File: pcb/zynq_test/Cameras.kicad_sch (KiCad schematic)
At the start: 0 parts

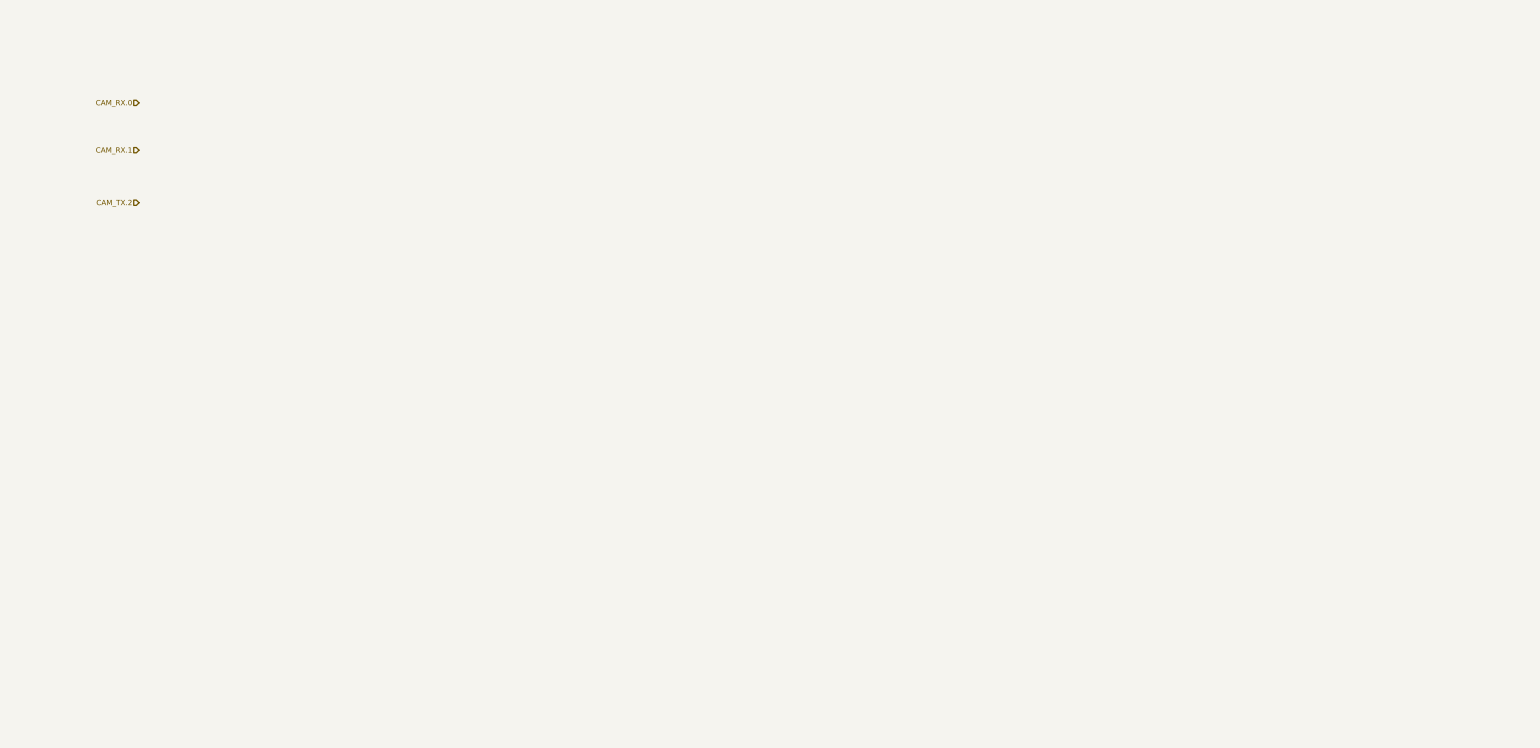
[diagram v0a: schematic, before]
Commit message: Added Cameras, changed SD card IC for skew reasons
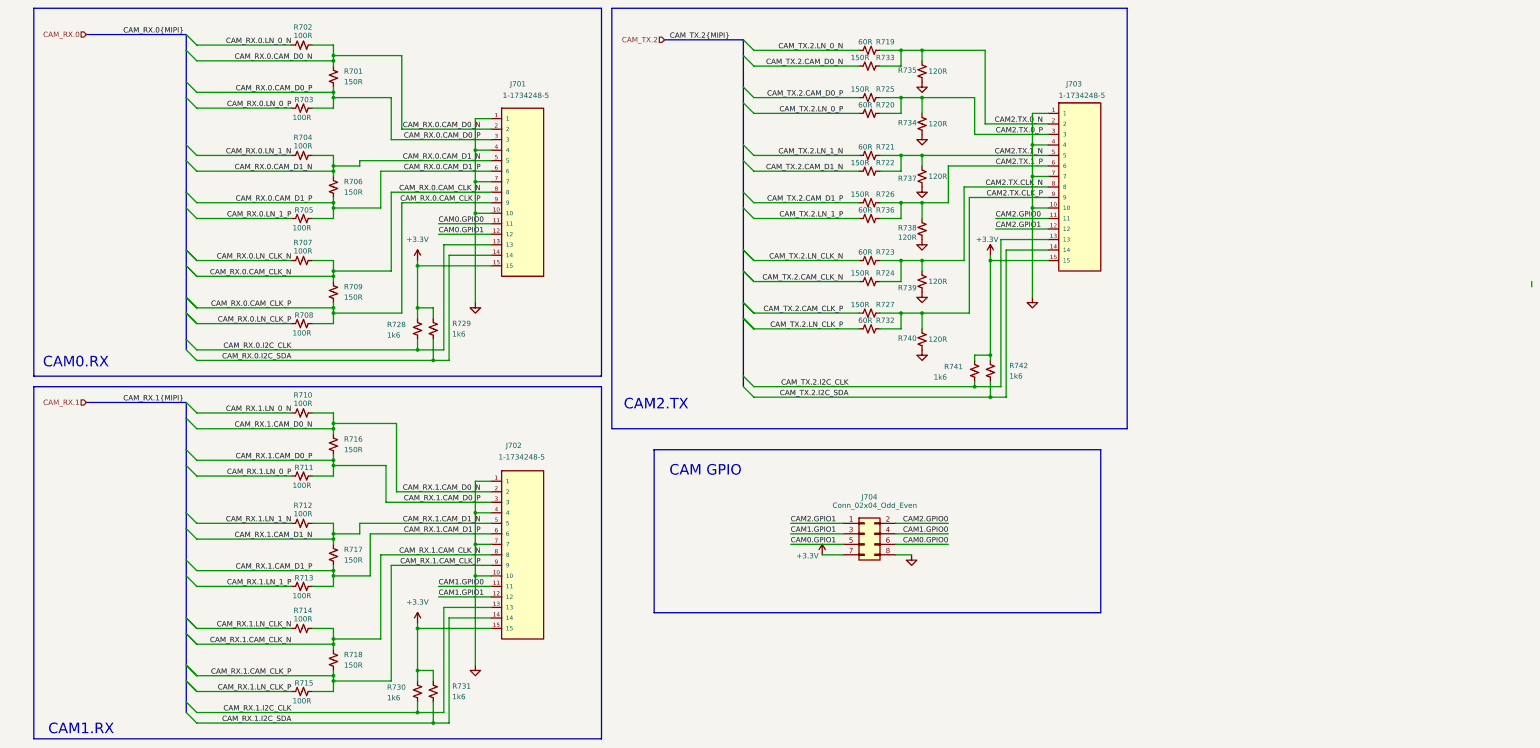
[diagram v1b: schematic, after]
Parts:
- added J701, J702, J703: 1-1734248-5, Camera:TE_1-1734248-5, symbol camera:1-1734248-5
- added J704: Conn_02x04_Odd_Even, symbol Connector_Generic:Conn_02x04_Odd_Even
- added R701, R706, R709, R716, R717, R718, R722, R724, R725, R726, R727, R733: 150R, symbol Device:R_Small_US
- added R702, R703, R704, R705, R707, R708, R710, R711, R712, R713, R714, R715: 100R, symbol Device:R_Small_US
- added R719, R720, R721, R723, R732, R736: 60R, symbol Device:R_Small_US
- added R728, R729, R730, R731, R741, R742: 1k6, symbol Device:R_Small_US
- added R734, R735, R737, R738, R739, R740: 120R, symbol Device:R_Small_US
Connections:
- new net +3.3V: J701.15, J701.15_1 (15__1), J702.15, J702.15_1 (15__1), J703.15, J703.15_1 (15__1), J704.7 (Pin_7), R728.1, R729.1, R730.1, R731.1, R741.1, R742.1
- new net CAM0.GPIO0: J701.11, J701.11_1 (11__1), J704.6 (Pin_6)
- new net CAM0.GPIO1: J701.12, J701.12_1 (12__1), J704.5 (Pin_5)
- new net CAM1.GPIO0: J702.11, J702.11_1 (11__1), J704.4 (Pin_4)
- new net CAM1.GPIO1: J702.12, J702.12_1 (12__1), J704.3 (Pin_3)
- new net CAM2.GPIO0: J703.11, J703.11_1 (11__1), J704.2 (Pin_2)
- new net CAM2.GPIO1: J703.12, J703.12_1 (12__1), J704.1 (Pin_1)
- new net CAM2.TX.0_N: J703.2, J703.2_1 (2__1), R719.2, R733.2, R735.2
- new net CAM2.TX.0_P: J703.3, J703.3_1 (3__1), R720.2, R725.2, R734.2
- new net CAM2.TX.1_N: J703.5, J703.5_1 (5__1), R721.2, R722.2, R737.2
- new net CAM2.TX.1_P: J703.6, J703.6_1 (6__1), R726.2, R736.2, R738.2
- new net CAM2.TX.CLK_N: J703.8, J703.8_1 (8__1), R723.2, R724.2, R739.2
- new net CAM2.TX.CLK_P: J703.9, J703.9_1 (9__1), R727.2, R732.2, R740.2
- new net CAM_RX.0.CAM_CLK_N: J701.8, J701.8_1 (8__1), R707.2, R709.1
- new net CAM_RX.0.CAM_CLK_P: J701.9, J701.9_1 (9__1), R708.2, R709.2
- new net CAM_RX.0.CAM_D0_N: J701.2, J701.2_1 (2__1), R701.1, R702.2
- new net CAM_RX.0.CAM_D0_P: J701.3, J701.3_1 (3__1), R701.2, R703.2
- new net CAM_RX.0.CAM_D1_N: J701.5, J701.5_1 (5__1), R704.2, R706.1
- new net CAM_RX.0.CAM_D1_P: J701.6, J701.6_1 (6__1), R705.2, R706.2
- new net CAM_RX.0.I2C_CLK: J701.13, J701.13_1 (13__1), R728.2
- new net CAM_RX.0.I2C_SDA: J701.14, J701.14_1 (14__1), R729.2
- new net CAM_RX.0.LN_0_N: R702.1
- new net CAM_RX.0.LN_0_P: R703.1
- new net CAM_RX.0.LN_1_N: R704.1
- new net CAM_RX.0.LN_1_P: R705.1
- new net CAM_RX.0.LN_CLK_N: R707.1
- new net CAM_RX.0.LN_CLK_P: R708.1
- new net CAM_RX.1.CAM_CLK_N: J702.8, J702.8_1 (8__1), R714.2, R718.1
- new net CAM_RX.1.CAM_CLK_P: J702.9, J702.9_1 (9__1), R715.2, R718.2
- new net CAM_RX.1.CAM_D0_N: J702.2, J702.2_1 (2__1), R710.2, R716.1
- new net CAM_RX.1.CAM_D0_P: J702.3, J702.3_1 (3__1), R711.2, R716.2
- new net CAM_RX.1.CAM_D1_N: J702.5, J702.5_1 (5__1), R712.2, R717.1
- new net CAM_RX.1.CAM_D1_P: J702.6, J702.6_1 (6__1), R713.2, R717.2
- new net CAM_RX.1.I2C_CLK: J702.13, J702.13_1 (13__1), R730.2
- new net CAM_RX.1.I2C_SDA: J702.14, J702.14_1 (14__1), R731.2
- new net CAM_RX.1.LN_0_N: R710.1
- new net CAM_RX.1.LN_0_P: R711.1
- new net CAM_RX.1.LN_1_N: R712.1
- new net CAM_RX.1.LN_1_P: R713.1
- new net CAM_RX.1.LN_CLK_N: R714.1
- new net CAM_RX.1.LN_CLK_P: R715.1
- new net CAM_TX.2.CAM_CLK_N: R724.1
- new net CAM_TX.2.CAM_CLK_P: R727.1
- new net CAM_TX.2.CAM_D0_N: R733.1
- new net CAM_TX.2.CAM_D0_P: R725.1
- new net CAM_TX.2.CAM_D1_N: R722.1
- new net CAM_TX.2.CAM_D1_P: R726.1
- new net CAM_TX.2.I2C_CLK: J703.13, J703.13_1 (13__1), R741.2
- new net CAM_TX.2.I2C_SDA: J703.14, J703.14_1 (14__1), R742.2
- new net CAM_TX.2.LN_0_N: R719.1
- new net CAM_TX.2.LN_0_P: R720.1
- new net CAM_TX.2.LN_1_N: R721.1
- new net CAM_TX.2.LN_1_P: R736.1
- new net CAM_TX.2.LN_CLK_N: R723.1
- new net CAM_TX.2.LN_CLK_P: R732.1
- new net GND: J701.1, J701.10, J701.10_1 (10__1), J701.1_1 (1__1), J701.4, J701.4_1 (4__1), J701.7, J701.7_1 (7__1), J702.1, J702.10, J702.10_1 (10__1), J702.1_1 (1__1), J702.4, J702.4_1 (4__1), J702.7, J702.7_1 (7__1), J703.1, J703.10, J703.10_1 (10__1), J703.1_1 (1__1), J703.4, J703.4_1 (4__1), J703.7, J703.7_1 (7__1), J704.8 (Pin_8), R734.1, R735.1, R737.1, R738.1, R739.1, R740.1
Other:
- note added: "CAM GPIO"
- note added: "CAM0.RX"
- note added: "CAM1.RX"
- note added: "CAM2.TX"

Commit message: Connected DDR3, cleaned up some thing
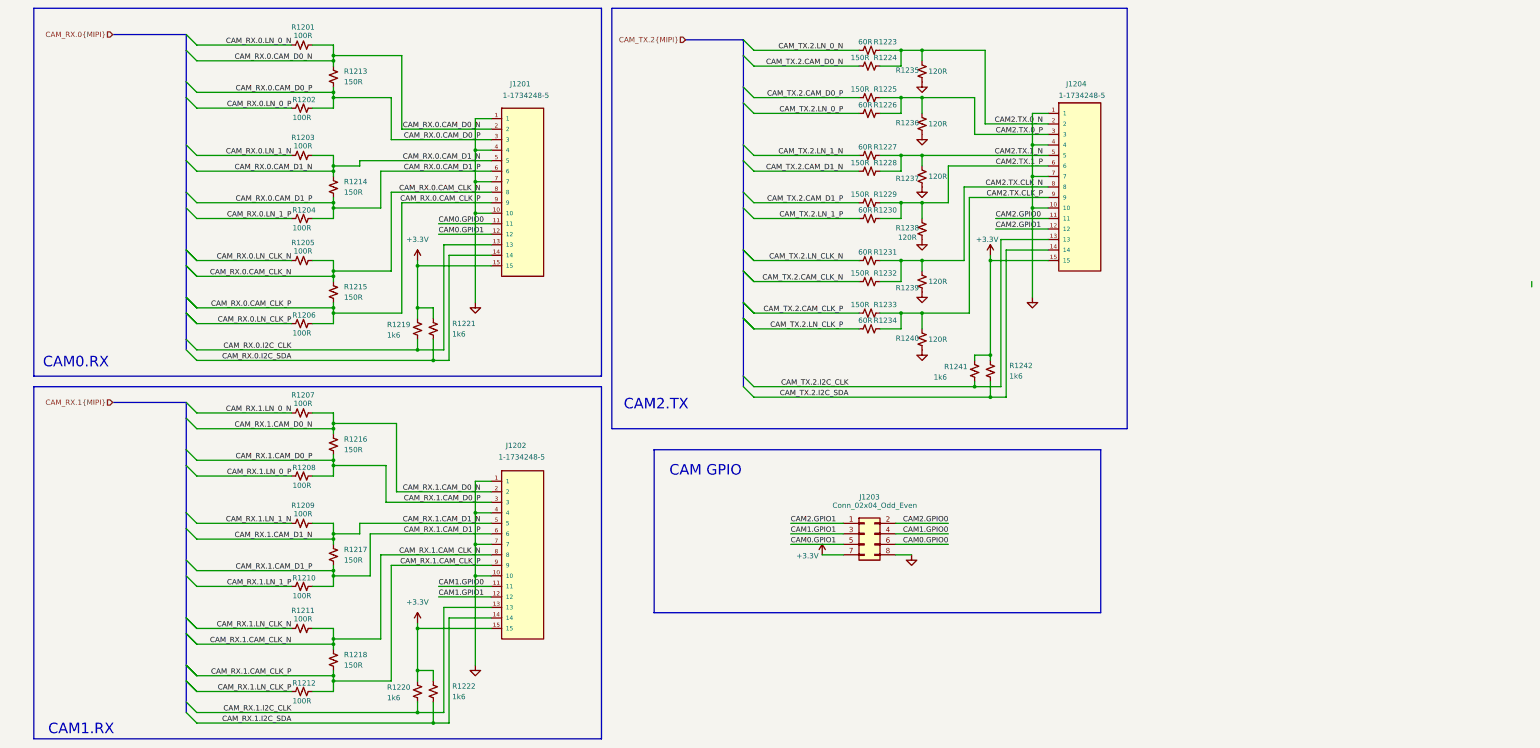
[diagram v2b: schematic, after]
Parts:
- J1201: renamed from J701; footprint Camera:TE_1-1734248-5 -> 1-1734248-5:TE_1-1734248-5
- J1202: renamed from J702; footprint Camera:TE_1-1734248-5 -> 1-1734248-5:TE_1-1734248-5
- J1204: renamed from J703; footprint Camera:TE_1-1734248-5 -> 1-1734248-5:TE_1-1734248-5
- renumbered J704 to J1203, R702 to R1201, R703 to R1202, R704 to R1203, R705 to R1204, R707 to R1205, R708 to R1206, R710 to R1207, R711 to R1208, R712 to R1209, R713 to R1210, R714 to R1211, R715 to R1212, R701 to R1213, R706 to R1214, R709 to R1215, R716 to R1216, R717 to R1217, R718 to R1218, R728 to R1219, R730 to R1220, R729 to R1221, R731 to R1222, R719 to R1223, R733 to R1224, R725 to R1225, R720 to R1226, R721 to R1227, R722 to R1228, R726 to R1229, R736 to R1230, R723 to R1231, R724 to R1232, R727 to R1233, R732 to R1234, R735 to R1235, R734 to R1236, R737 to R1237, R738 to R1238, R739 to R1239, R740 to R1240, R741 to R1241, R742 to R1242

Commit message: Finished Power Supply
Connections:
- net +3.3V renamed +3V3
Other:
- title: (none) -> Camera
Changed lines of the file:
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@@
 	(paper "A4")
 	(title_block
-		(date "2025-09-06")
-		(rev "v1.0")
+		(title "Camera")
+		(date "2025-09-13")
+		(rev "A")
 	)
 	(bus_alias "MIPI"
@@
 	(wire
 		(pts
-			(xy 379.73 86.36) (xy 379.73 85.09)
-		)
-		(stroke
-			(width 0)
-			(type default)
-		)
-	)
-	(wire
-		(pts
 			(xy 85.09 95.25) (xy 90.17 95.25)
 		)
@@
 			)
 		)
-		(property "Value" "+3.3V"
+		(property "Value" "+3V3"
 			(at 110.49 74.93 0)
 			(effects
@@
 			)
 		)
-		(property "Value" "+3.3V"
+		(property "Value" "+3V3"
 			(at 204.724 151.384 0)
 			(effects
@@
 			)
 		)
-		(property "Value" "+3.3V"
+		(property "Value" "+3V3"
 			(at 248.158 74.93 0)
 			(effects
@@
 			)
 		)
-		(property "Value" "+3.3V"
+		(property "Value" "+3V3"
 			(at 110.49 162.56 0)
 			(effects

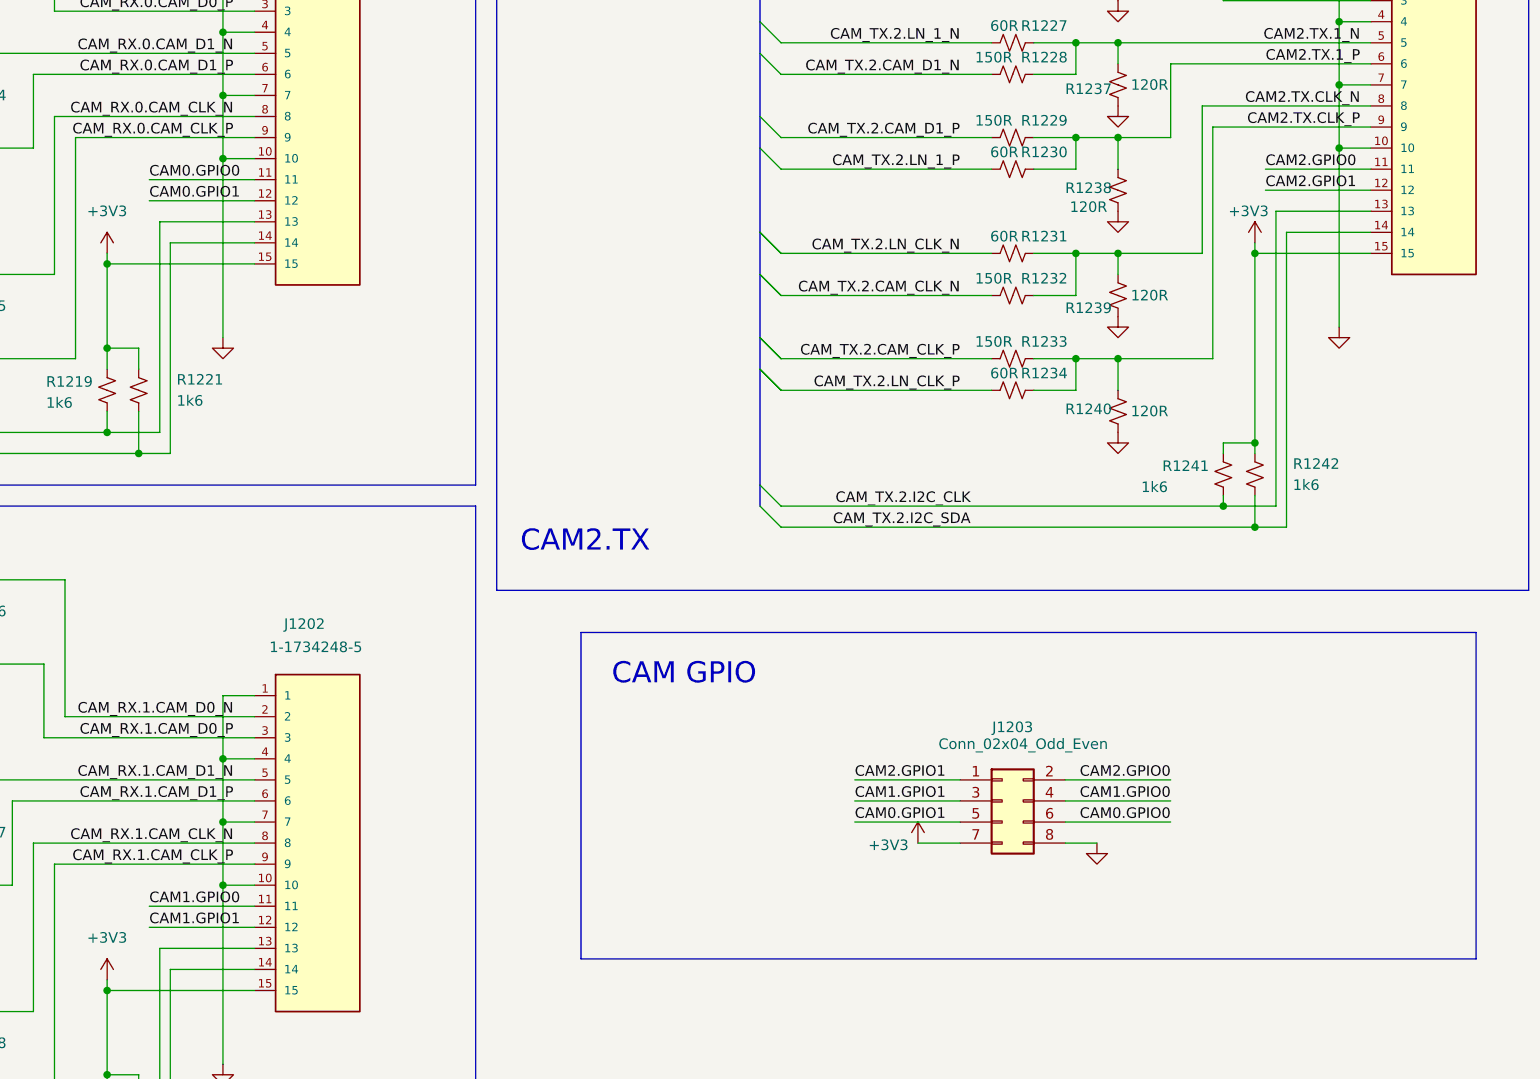
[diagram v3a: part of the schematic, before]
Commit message: Finished most of the schematic, will start routing soon
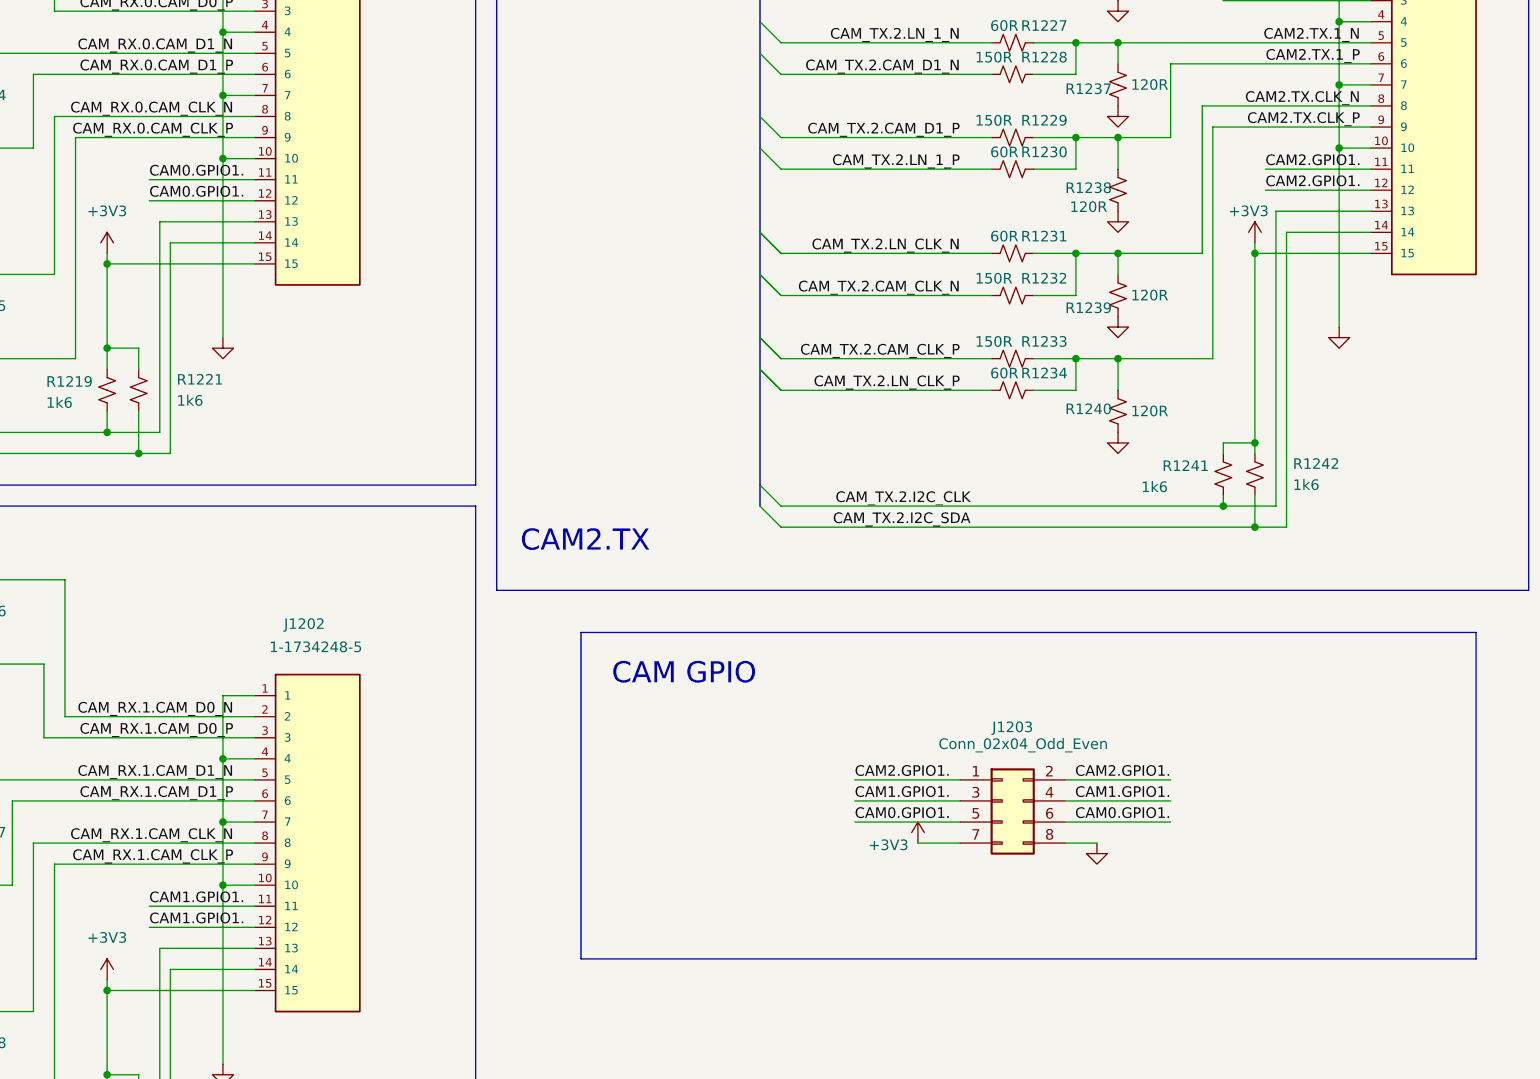
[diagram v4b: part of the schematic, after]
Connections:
- net CAM0.GPIO1 is gone; now on net CAM0.GPIO1.: J1201.12, J1201.12_1 (12__1), J1203.5 (Pin_5)
- net CAM1.GPIO1 is gone; now on net CAM1.GPIO1.: J1202.12, J1202.12_1 (12__1), J1203.3 (Pin_3)
- net CAM2.GPIO1 is gone; now on net CAM2.GPIO1.: J1203.1 (Pin_1), J1204.12, J1204.12_1 (12__1)
- net CAM0.GPIO0 renamed CAM0.GPIO1.
- net CAM1.GPIO0 renamed CAM1.GPIO1.
- net CAM2.GPIO0 renamed CAM2.GPIO1.
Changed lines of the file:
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@@
 		)
 	)
-	(label "CAM2.GPIO1"
+	(label "CAM2.GPIO1."
 		(at 250.19 72.39 0)
 		(effects
@@
 		)
 	)
-	(label "CAM1.GPIO1"
+	(label "CAM1.GPIO1."
 		(at 200.66 146.05 0)
 		(effects
@@
 		)
 	)
-	(label "CAM1.GPIO1"
+	(label "CAM1.GPIO1."
 		(at 115.57 161.29 0)
 		(effects
@@
 		)
 	)
-	(label "CAM0.GPIO1"
+	(label "CAM0.GPIO1."
 		(at 200.66 148.59 0)
 		(effects
@@
 		)
 	)
-	(label "CAM2.GPIO0"
+	(label "CAM2.GPIO1."
 		(at 250.19 69.85 0)
 		(effects
@@
 		)
 	)
-	(label "CAM2.GPIO1"
+	(label "CAM2.GPIO1."
 		(at 200.66 143.51 0)
 		(effects
@@
 		)
 	)
-	(label "CAM1.GPIO0"
+	(label "CAM1.GPIO1."
 		(at 115.57 158.75 0)
 		(effects
@@
 		)
 	)
-	(label "CAM2.GPIO0"
+	(label "CAM2.GPIO1."
 		(at 238.76 143.51 180)
 		(effects
@@
 		)
 	)
-	(label "CAM1.GPIO0"
+	(label "CAM1.GPIO1."
 		(at 238.76 146.05 180)
 		(effects
@@
 		)
 	)
-	(label "CAM0.GPIO0"
+	(label "CAM0.GPIO1."
 		(at 238.76 148.59 180)
 		(effects
@@
 		)
 	)
-	(label "CAM0.GPIO1"
+	(label "CAM0.GPIO1."
 		(at 115.57 73.66 0)
 		(effects
@@
 		)
 	)
-	(label "CAM0.GPIO0"
+	(label "CAM0.GPIO1."
 		(at 115.57 71.12 0)
 		(effects

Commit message: Finished to first ddr ic
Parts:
- J1201, J1202, J1204: footprint 1-1734248-5:TE_1-1734248-5 -> (none)
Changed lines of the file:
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@@
 			)
 		)
-		(property "Footprint" "1-1734248-5:TE_1-1734248-5"
+		(property "Footprint" ""
 			(at 267.716 37.084 0)
 			(effects
@@
 			)
 		)
-		(property "Footprint" "1-1734248-5:TE_1-1734248-5"
+		(property "Footprint" ""
 			(at 133.096 38.354 0)
 			(effects
@@
 			)
 		)
-		(property "Footprint" "1-1734248-5:TE_1-1734248-5"
+		(property "Footprint" ""
 			(at 133.096 125.984 0)
 			(effects
